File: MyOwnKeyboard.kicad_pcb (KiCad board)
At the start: 2 copper layers, 461 parts, among them Q1 2N7000, SW1 SW_SPST, SW10 SW_SPST, SW100 SW_SPST, SW101 SW_SPST, SW102 SW_SPST, SW103 SW_SPST, SW104 SW_SPST, SW105 SW_SPST, SW106 SW_SPST, SW107 SW_SPST, SW108 SW_SPST, SW109 SW_SPST, SW11 SW_SPST, SW110 SW_SPST, SW111 SW_SPST, SW112 SW_SPST, SW113 SW_SPST, SW114 SW_SPST, SW12 SW_SPST, SW13 SW_SPST, SW14 SW_SPST, SW15 SW_SPST, SW16 SW_SPST, SW17 SW_SPST, SW18 SW_SPST, SW19 SW_SPST, SW2 SW_SPST, SW20 SW_SPST, SW21 SW_SPST, SW22 SW_SPST, SW23 SW_SPST, SW24 SW_SPST, SW25 SW_SPST, SW26 SW_SPST, SW27 SW_SPST, SW28 SW_SPST, SW29 SW_SPST, SW3 SW_SPST, SW30 SW_SPST, SW31 SW_SPST, SW32 SW_SPST, SW33 SW_SPST, SW34 SW_SPST, SW35 SW_SPST, SW36 SW_SPST, SW37 SW_SPST, SW38 SW_SPST, SW39 SW_SPST, SW4 SW_SPST, SW40 SW_SPST, SW41 SW_SPST, SW42 SW_SPST, SW43 SW_SPST, SW44 SW_SPST, SW45 SW_SPST, SW46 SW_SPST, SW47 SW_SPST, SW48 SW_SPST, SW49 SW_SPST, SW5 SW_SPST, SW50 SW_SPST, SW51 SW_SPST, SW52 SW_SPST, SW53 SW_SPST, SW54 SW_SPST, SW55 SW_SPST, SW56 SW_SPST, SW57 SW_SPST, SW58 SW_SPST, SW59 SW_SPST, SW6 SW_SPST, SW60 SW_SPST, SW61 SW_SPST, SW62 SW_SPST, SW63 SW_SPST, SW64 SW_SPST, SW65 SW_SPST, SW66 SW_SPST, SW67 SW_SPST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

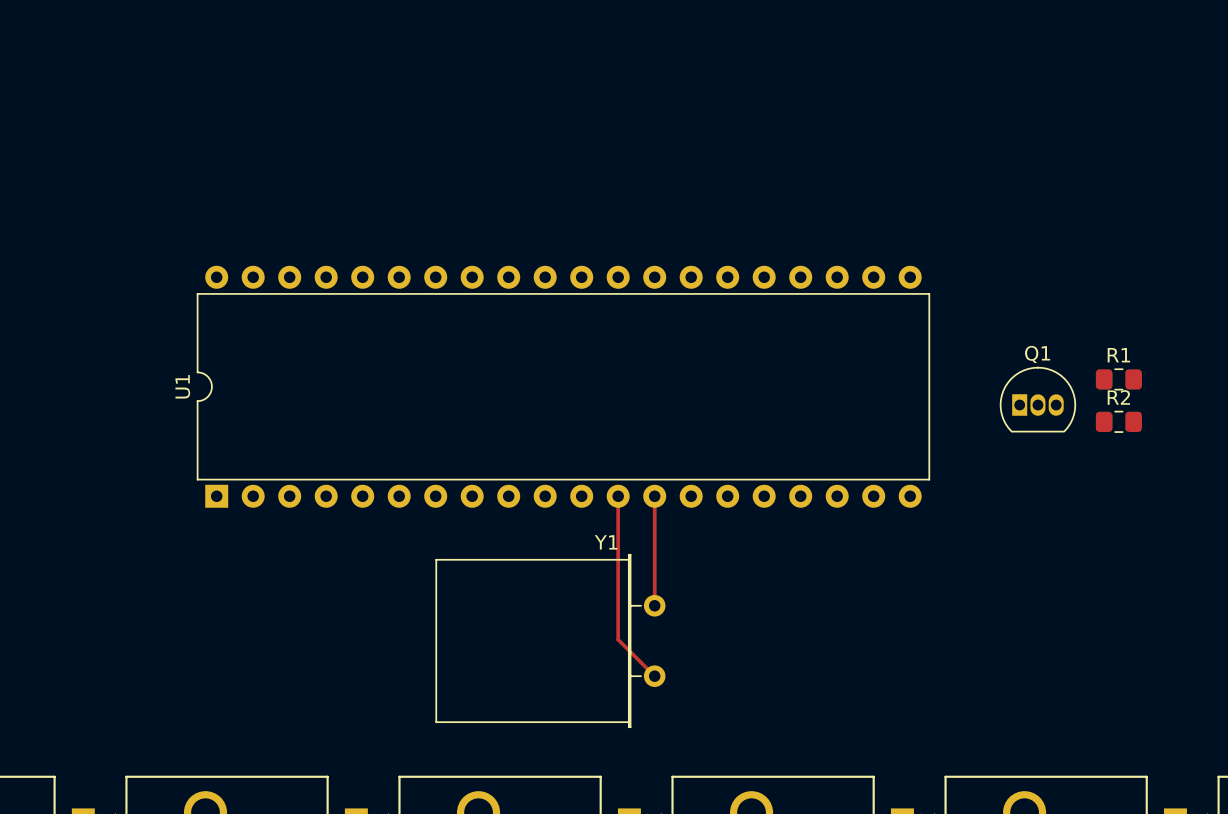
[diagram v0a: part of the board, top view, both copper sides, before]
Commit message: Add NUM/CAPSLOCK indicators, finalise components
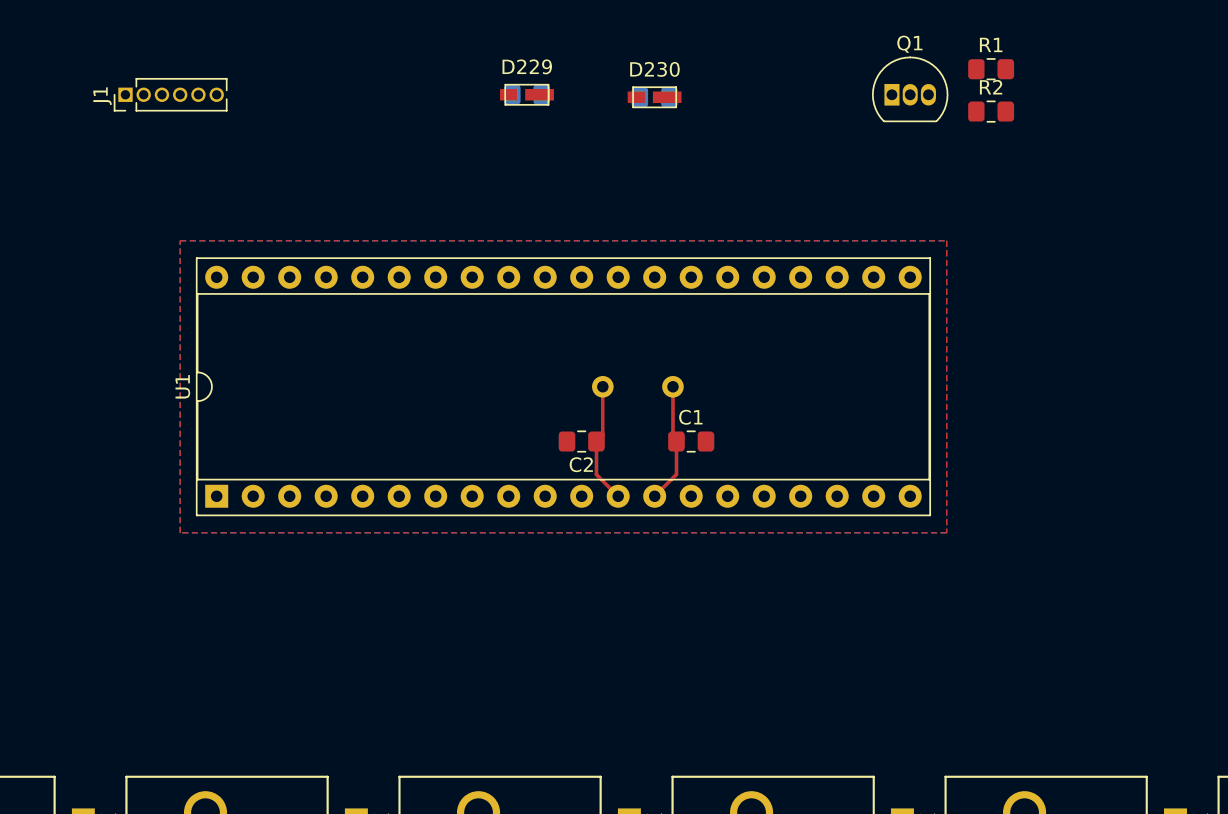
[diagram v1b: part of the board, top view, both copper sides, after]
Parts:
- added C1: 30pF, Capacitor_SMD:C_0805_2012Metric_Pad1.15x1.40mm_HandSolder, F.Cu at (207.0, 63.5)
- added C2: 30pF, Capacitor_SMD:C_0805_2012Metric_Pad1.15x1.40mm_HandSolder, F.Cu at (199.4, 63.5)
- added D229: NUMLOCK, MyOwnKeyboard:158301250, F.Cu at (195.6, 39.4)
- added D230: CAPSLOCK, MyOwnKeyboard:158301250, F.Cu at (204.5, 39.5)
- added J1: Mini-DIN-6, Connector_PinHeader_1.27mm:PinHeader_1x06_P1.27mm_Vertical, F.Cu at (167.6, 39.4)
- added R117: 2.3k, Resistor_SMD:R_0805_2012Metric_Pad1.15x1.40mm_HandSolder, B.Cu at (195.6, 39.4)
- added R118: 2.3k, Resistor_SMD:R_0805_2012Metric_Pad1.15x1.40mm_HandSolder, B.Cu at (204.5, 39.5)
- Q1: value 2N7000 -> RFD14N05L
- U1: footprint Package_DIP:DIP-40_W15.24mm -> Package_DIP:DIP-40_W15.24mm_Socket
- Y1: footprint Crystal:Crystal_HC49-U_Horizontal -> Crystal:Crystal_HC49-U_Vertical; moved to B.Cu
- moved Q1 23.3 mm to (221.0, 39.4)
- moved R2 23.3 mm to (227.9, 40.5)
- moved R1 23.3 mm to (227.9, 37.6)
- moved Y1 15.3 mm to (205.7, 59.7), turned to 180 degrees
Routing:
- net Net-(C2-Pad1): track 13.6 -> 8.43 mm
- net Net-(C1-Pad1): track 7.62 -> 8.35 mm
- added copper zone on B.Cu, net Earth
- added copper zone on F.Cu, net Earth

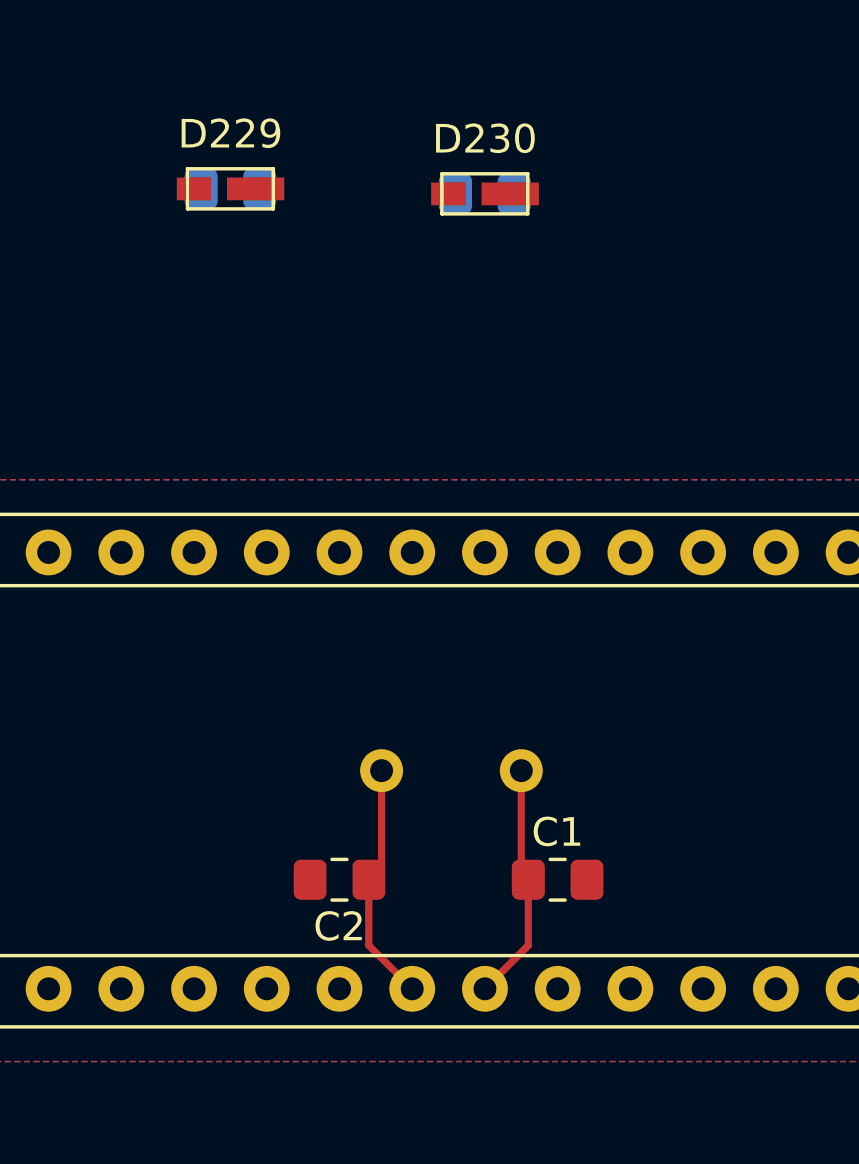
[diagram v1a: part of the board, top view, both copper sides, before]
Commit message: Removed crystal, finalised design
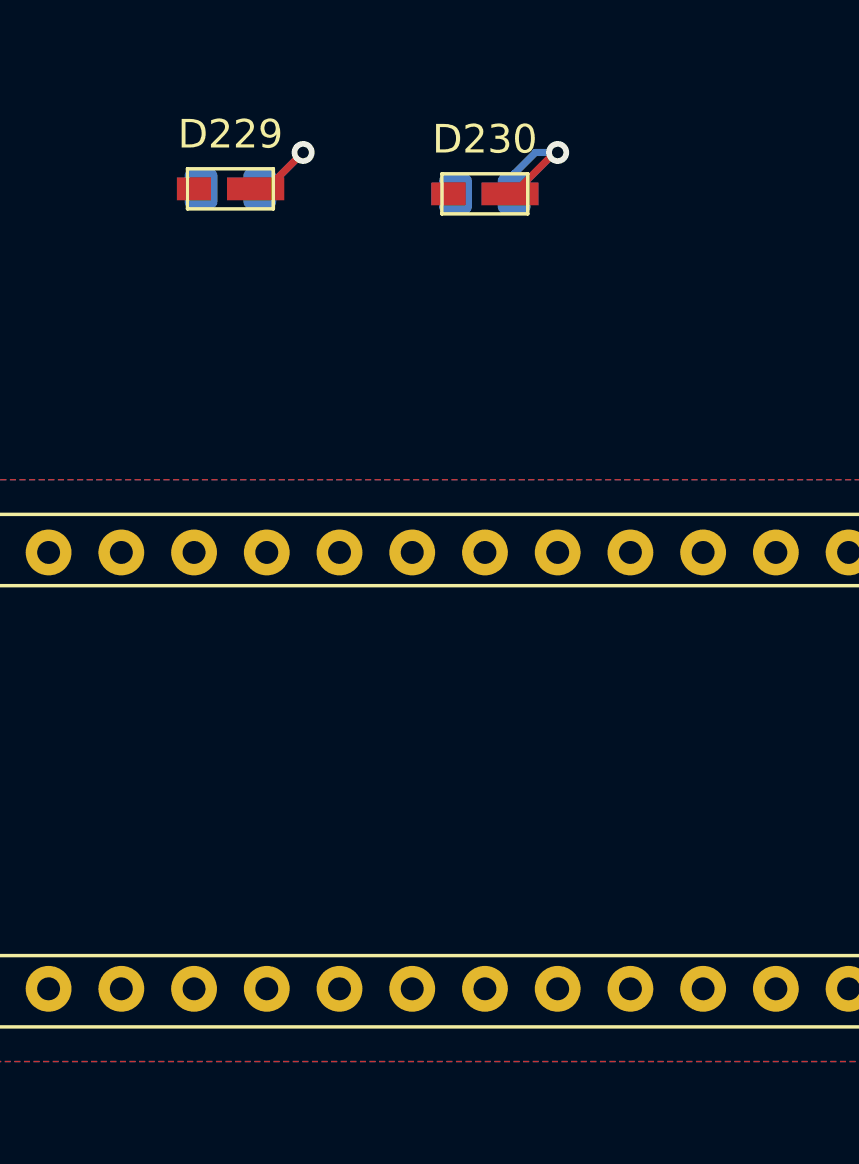
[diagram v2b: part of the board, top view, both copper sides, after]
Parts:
- removed C1, C2: 30pF, Capacitor_SMD:C_0805_2012Metric_Pad1.15x1.40mm_HandSolder
- removed Y1: 20MHz, Crystal:Crystal_HC49-U_Vertical
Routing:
- net Net-(U1-Pad12): track 8.43 -> 0.00 mm
- net Net-(U1-Pad13): track 8.35 -> 0.00 mm
- net Net-(D230-Pad1): track 0.00 -> 4.67 mm, vias 0 -> 1
- net Net-(D229-Pad1): track 0.00 -> 4.11 mm, vias 0 -> 1
